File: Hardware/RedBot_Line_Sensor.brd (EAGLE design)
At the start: 7.6 x 24.1 mm, 9 parts, among them U1 QRE1113

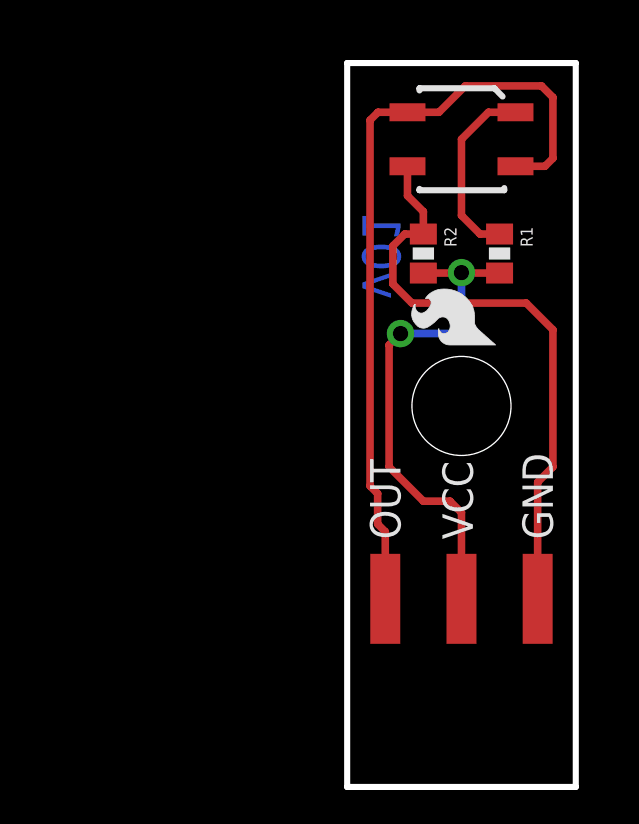
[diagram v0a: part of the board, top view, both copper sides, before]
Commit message: Change to Rev 10 for release  - flipped connector to bottom side of board  - change revision number
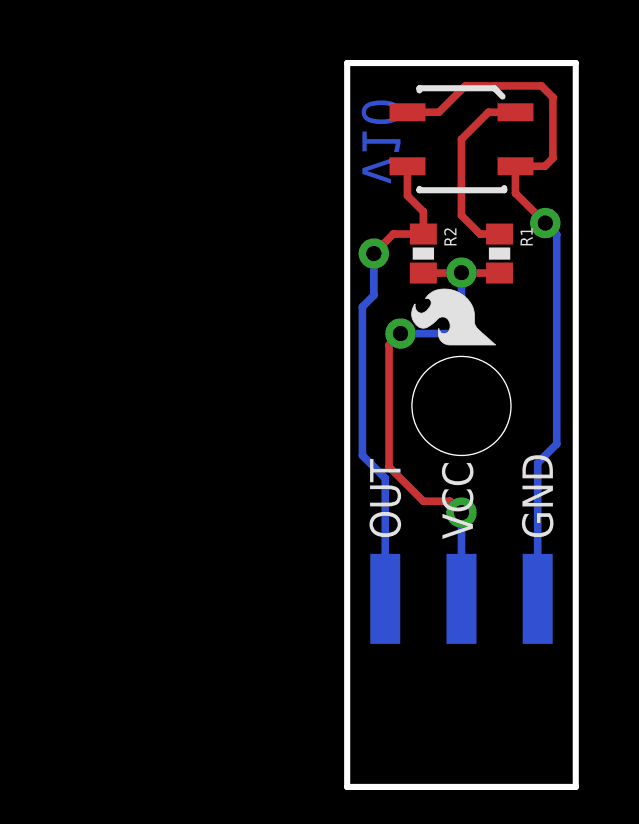
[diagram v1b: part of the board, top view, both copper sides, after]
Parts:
- flipped JP1 to the bottom
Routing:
- net N$2: track 20.1 -> 16.4 mm, vias 0 -> 1
- net GND: track 26.3 -> 24.0 mm, vias 0 -> 1
- net 5V: vias 2 -> 3
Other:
- board text added: "v10"
- board text removed: "v01"
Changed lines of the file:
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@@
 <wire x1="0" y1="24.13" x2="0" y2="0" width="0.2032" layer="20"/>
 <text x="-41.91" y="-16.51" size="1.778" layer="25" font="vector" ratio="15">M.Hord</text>
-<text x="0.508" y="16.256" size="1.27" layer="16" font="vector" ratio="15" rot="MR90">v01</text>
+<text x="0.508" y="20.066" size="1.27" layer="16" font="vector" ratio="15" rot="MR90">v10</text>
 </plain>
 <attributes>
@@
 </class>
 </classes>
-<designrules name="default">
+<designrules name="Sparkfun">
 <description language="en">&lt;b&gt;EAGLE Design Rules&lt;/b&gt;
 &lt;p&gt;
@@
 may have different requirements, so please make the
 necessary adjustments and save your customized
-design rules under a new name.
-</description>
+design rules under a new name.</description>
 <param name="layerSetup" value="(1*16)"/>
 <param name="mtCopper" value="0.035mm 0.035mm 0.035mm 0.035mm 0.035mm 0.035mm 0.035mm 0.035mm 0.035mm 0.035mm 0.035mm 0.035mm 0.035mm 0.035mm 0.035mm 0.035mm"/>
@@
 <param name="mdViaViaSameLayer" value="8mil"/>
 <param name="mnLayersViaInSmd" value="2"/>
-<param name="mdCopperDimension" value="40mil"/>
+<param name="mdCopperDimension" value="8mil"/>
 <param name="mdDrill" value="8mil"/>
 <param name="mdSmdStop" value="0mil"/>
-<param name="msWidth" value="10mil"/>
-<param name="msDrill" value="0.6mm"/>
+<param name="msWidth" value="8mil"/>
+<param name="msDrill" value="20mil"/>
 <param name="msMicroVia" value="9.99mm"/>
 <param name="msBlindViaRatio" value="0.5"/>
@@
 <param name="rvMicroViaOuter" value="0.25"/>
 <param name="rvMicroViaInner" value="0.25"/>
-<param name="rlMinPadTop" value="10mil"/>
+<param name="rlMinPadTop" value="12mil"/>
 <param name="rlMaxPadTop" value="20mil"/>
 <param name="rlMinPadInner" value="10mil"/>
 <param name="rlMaxPadInner" value="20mil"/>
-<param name="rlMinPadBottom" value="10mil"/>
+<param name="rlMinPadBottom" value="12mil"/>
 <param name="rlMaxPadBottom" value="20mil"/>
-<param name="rlMinViaOuter" value="8mil"/>
+<param name="rlMinViaOuter" value="10mil"/>
 <param name="rlMaxViaOuter" value="20mil"/>
-<param name="rlMinViaInner" value="8mil"/>
+<param name="rlMinViaInner" value="10mil"/>
 <param name="rlMaxViaInner" value="20mil"/>
 <param name="rlMinMicroViaOuter" value="4mil"/>
@@
 <param name="mlMinCreamFrame" value="0mil"/>
 <param name="mlMaxCreamFrame" value="0mil"/>
-<param name="mlViaStopLimit" value="0mil"/>
+<param name="mlViaStopLimit" value="20mil"/>
 <param name="srRoundness" value="0"/>
 <param name="srMinRoundness" value="0mil"/>
@@
 <param name="checkRestrict" value="1"/>
 <param name="useDiameter" value="13"/>
-<param name="maxErrors" value="999999"/>
+<param name="maxErrors" value="50"/>
 </designrules>
 <autorouter>
@@
 <attribute name="PROD_ID" value="RES-00824" x="-22.86" y="-20.32" size="1.778" layer="27" rot="R270" display="off"/>
 </element>
-<element name="JP1" library="SparkFun-Connectors" package="1X03_SMD_RA_MALE" value="" x="3.81" y="1.27">
-<attribute name="PROD_ID" value="CONN-10925" x="3.81" y="1.27" size="1.778" layer="27" display="off"/>
+<element name="JP1" library="SparkFun-Connectors" package="1X03_SMD_RA_MALE" value="" x="3.81" y="1.27" rot="MR0">
+<attribute name="PROD_ID" value="CONN-10925" x="3.81" y="1.27" size="1.778" layer="28" rot="MR0" display="off"/>
 </element>
 <element name="STANDOFF1" library="SparkFun-Electromechanical" package="STAND-OFF" value="STAND-OFF" x="3.81" y="12.7"/>
@@
 <wire x1="2.54" y1="19.177" x2="2.01" y2="19.707" width="0.254" layer="1"/>
 <wire x1="2.01" y1="20.69" x2="2.01" y2="19.707" width="0.254" layer="1"/>
-<wire x1="2.54" y1="18.43" x2="1.92" y2="18.43" width="0.254" layer="1"/>
-<wire x1="1.92" y1="18.43" x2="1.524" y2="18.034" width="0.254" layer="1"/>
-<wire x1="1.524" y1="18.034" x2="1.524" y2="16.764" width="0.254" layer="1"/>
-<wire x1="1.524" y1="16.764" x2="2.159" y2="16.129" width="0.254" layer="1"/>
-<wire x1="2.159" y1="16.129" x2="5.969" y2="16.129" width="0.254" layer="1"/>
-<wire x1="5.969" y1="16.129" x2="6.858" y2="15.24" width="0.254" layer="1"/>
-<wire x1="6.858" y1="15.24" x2="6.858" y2="10.668" width="0.254" layer="1"/>
-<wire x1="6.858" y1="10.668" x2="6.35" y2="10.16" width="0.254" layer="1"/>
-<wire x1="6.35" y1="10.16" x2="6.35" y2="6.27" width="0.254" layer="1"/>
+<wire x1="1.27" y1="6.27" x2="1.27" y2="10.287" width="0.254" layer="16"/>
+<wire x1="1.27" y1="10.287" x2="0.508" y2="11.049" width="0.254" layer="16"/>
+<wire x1="2.54" y1="18.43" x2="1.539" y2="18.43" width="0.254" layer="1"/>
+<wire x1="1.539" y1="18.43" x2="0.889" y2="17.78" width="0.254" layer="1"/>
+<via x="0.889" y="17.78" extent="1-16" drill="0.508"/>
+<wire x1="0.889" y1="17.78" x2="0.889" y2="16.383" width="0.254" layer="16"/>
+<wire x1="0.889" y1="16.383" x2="0.508" y2="16.002" width="0.254" layer="16"/>
+<wire x1="0.508" y1="16.002" x2="0.508" y2="11.049" width="0.254" layer="16"/>
 </signal>
 <signal name="5V">
@@
 <wire x1="2.54" y1="9.525" x2="3.429" y2="9.525" width="0.254" layer="1"/>
 <wire x1="3.429" y1="9.525" x2="3.81" y2="9.144" width="0.254" layer="1"/>
-<wire x1="3.81" y1="9.144" x2="3.81" y2="6.27" width="0.254" layer="1"/>
+<wire x1="3.81" y1="9.144" x2="3.81" y2="6.27" width="0.254" layer="16"/>
+<via x="3.81" y="9.144" extent="1-16" drill="0.508"/>
 </signal>
 <signal name="GND">
@@
 <contactref element="U1" pad="4"/>
 <contactref element="U1" pad="2"/>
-<wire x1="1.27" y1="6.27" x2="1.27" y2="8.509" width="0.254" layer="1"/>
-<wire x1="1.27" y1="8.509" x2="1.016" y2="8.763" width="0.254" layer="1"/>
-<wire x1="1.016" y1="8.763" x2="1.016" y2="9.779" width="0.254" layer="1"/>
-<wire x1="1.016" y1="9.779" x2="0.762" y2="10.033" width="0.254" layer="1"/>
-<wire x1="0.762" y1="10.033" x2="0.762" y2="22.225" width="0.254" layer="1"/>
-<wire x1="2.01" y1="22.49" x2="1.027" y2="22.49" width="0.254" layer="1"/>
-<wire x1="1.027" y1="22.49" x2="0.762" y2="22.225" width="0.254" layer="1"/>
 <wire x1="2.01" y1="22.49" x2="3.059" y2="22.49" width="0.254" layer="1"/>
 <wire x1="3.059" y1="22.49" x2="3.937" y2="23.368" width="0.254" layer="1"/>
@@
 <wire x1="6.858" y1="20.955" x2="6.593" y2="20.69" width="0.254" layer="1"/>
 <wire x1="5.61" y1="20.69" x2="6.593" y2="20.69" width="0.254" layer="1"/>
+<wire x1="6.35" y1="6.27" x2="6.35" y2="10.795" width="0.254" layer="16"/>
+<wire x1="6.35" y1="10.795" x2="6.985" y2="11.43" width="0.254" layer="16"/>
+<wire x1="6.985" y1="11.43" x2="6.985" y2="18.415" width="0.254" layer="16"/>
+<wire x1="6.985" y1="18.415" x2="6.604" y2="18.796" width="0.254" layer="16"/>
+<via x="6.604" y="18.796" extent="1-16" drill="0.508"/>
+<wire x1="6.604" y1="18.796" x2="5.61" y2="19.79" width="0.254" layer="1"/>
+<wire x1="5.61" y1="20.69" x2="5.61" y2="19.79" width="0.254" layer="1"/>
 </signal>
 </signals>
